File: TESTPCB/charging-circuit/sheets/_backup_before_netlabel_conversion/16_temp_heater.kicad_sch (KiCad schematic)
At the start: 13 parts, among them J1 2.54-1*6PHeader-RA, Q1 2N7002, Q2 CJQ4435, Q3 currentmirror, U9 ADS1115IDGSR

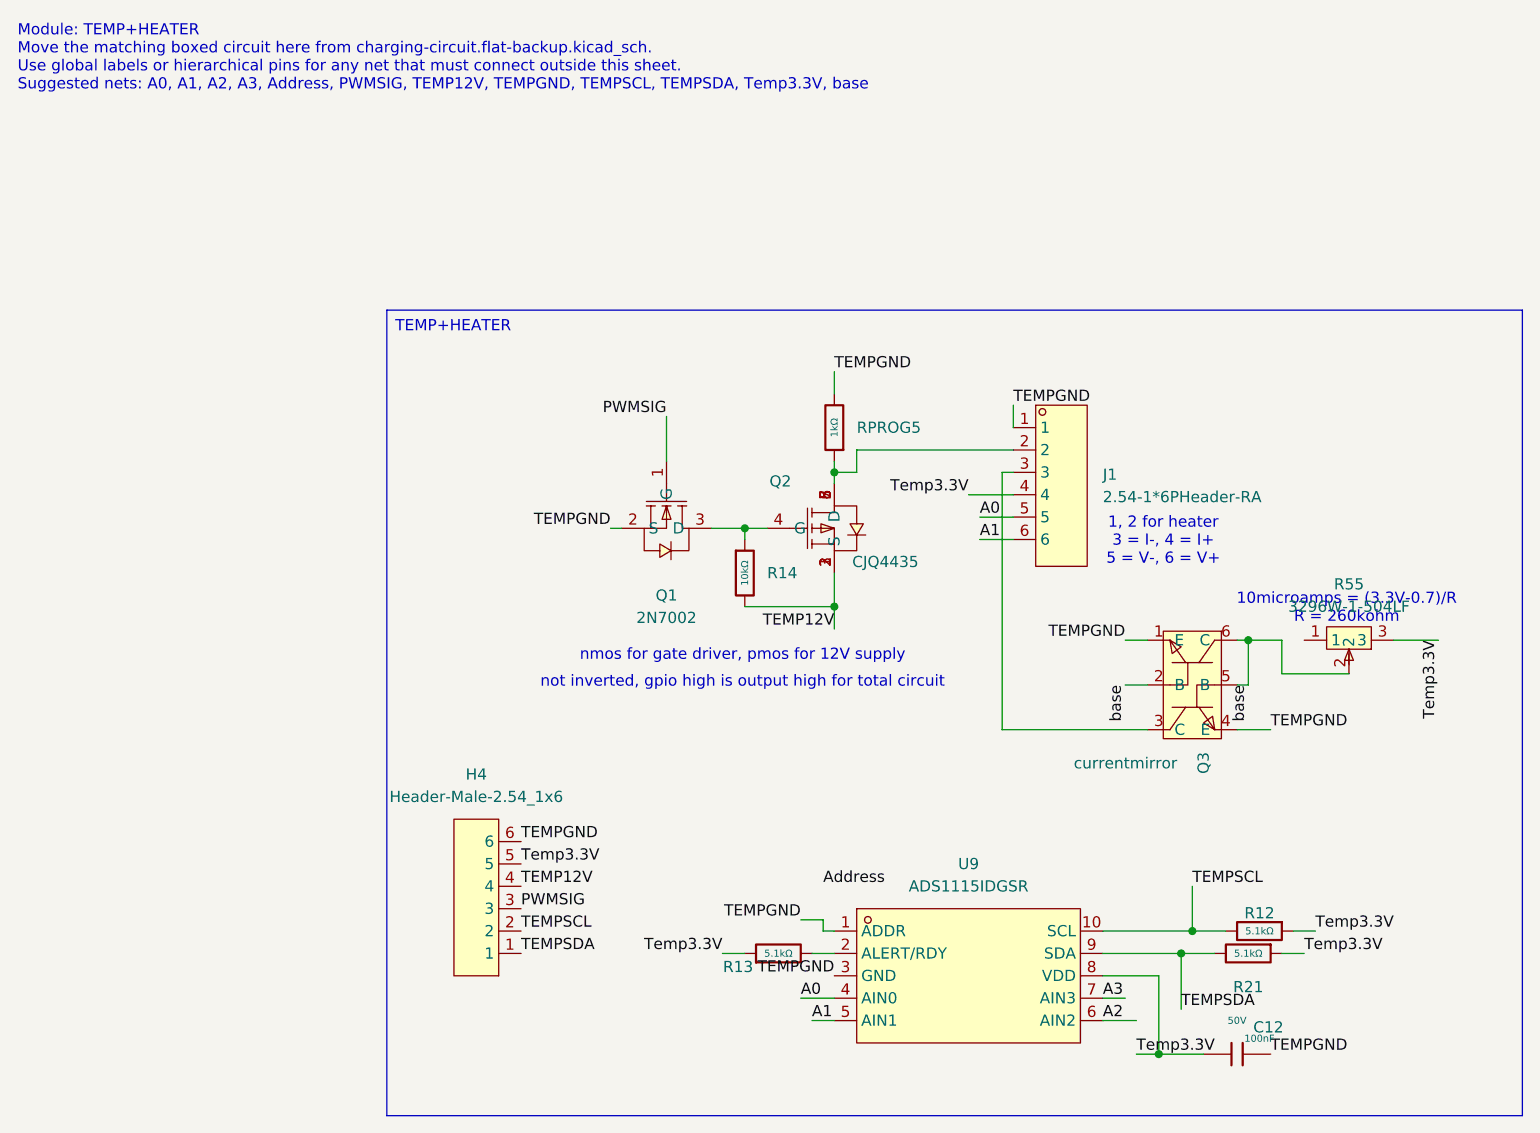
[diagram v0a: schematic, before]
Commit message: Fixed formatting issues, now the hierachal sheets are all labeled as net labels and when we want to expose their pins we will make them into hierchal or global pins
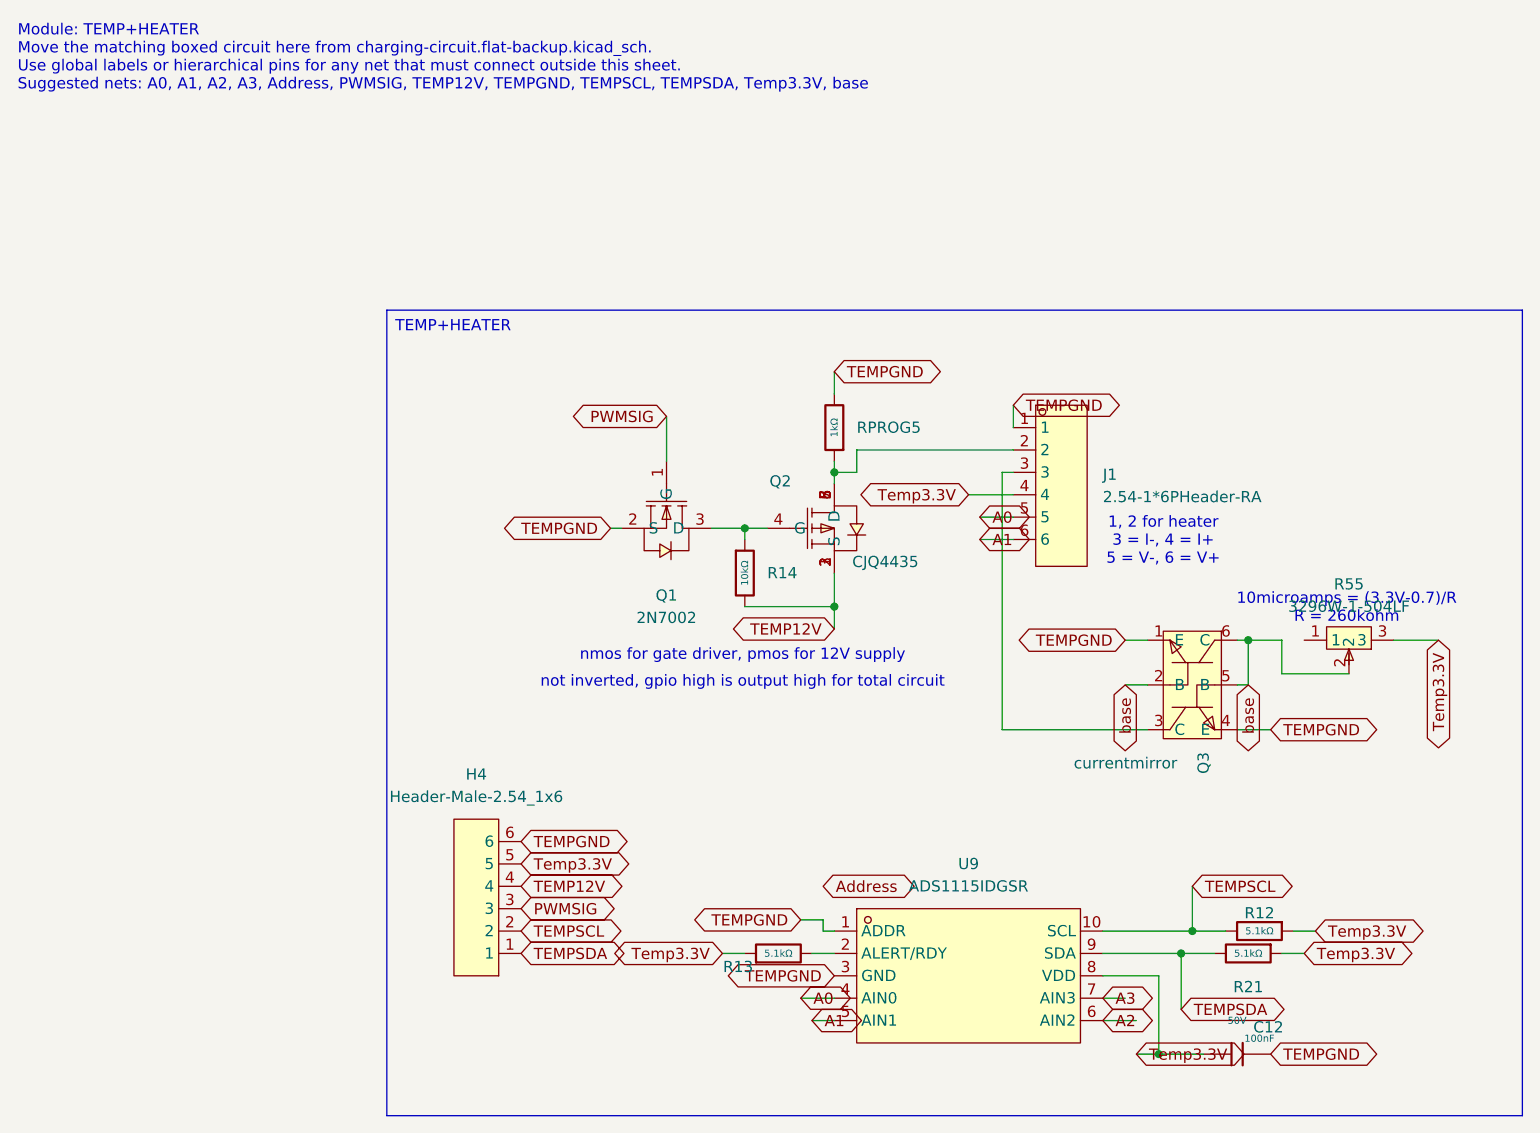
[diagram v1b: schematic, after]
